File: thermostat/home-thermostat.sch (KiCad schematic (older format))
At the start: 40 parts, among them J1 Thermosthat, U3 LM2574M-5, U4 LD1117S33TR_SOT223, U5 AT24C512

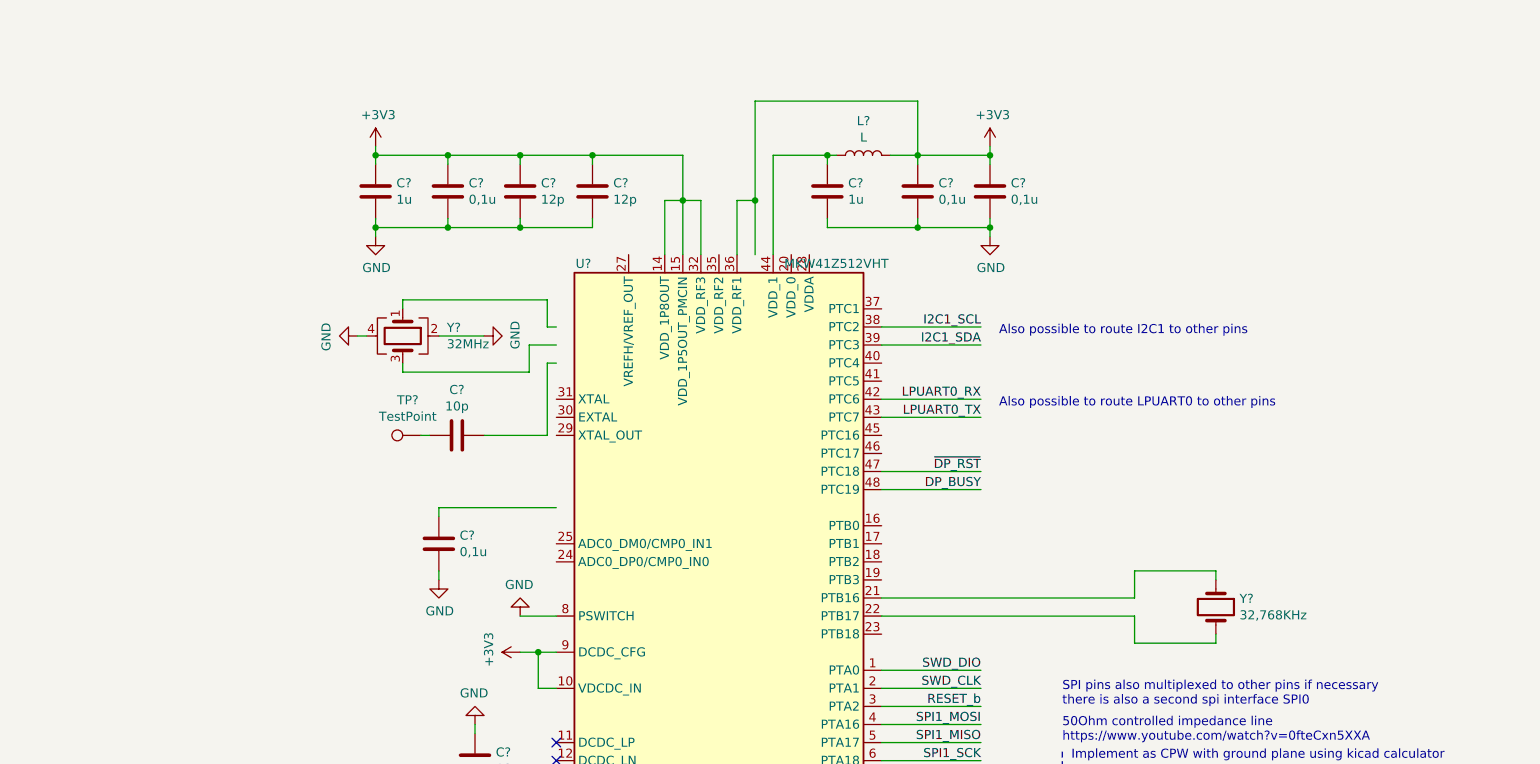
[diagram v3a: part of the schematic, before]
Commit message: Added some descriptions and the possibility to use VDD as reference voltage for the ADC of the MKW41Z. This can come handy if we want to use the ADC to measure voltages.
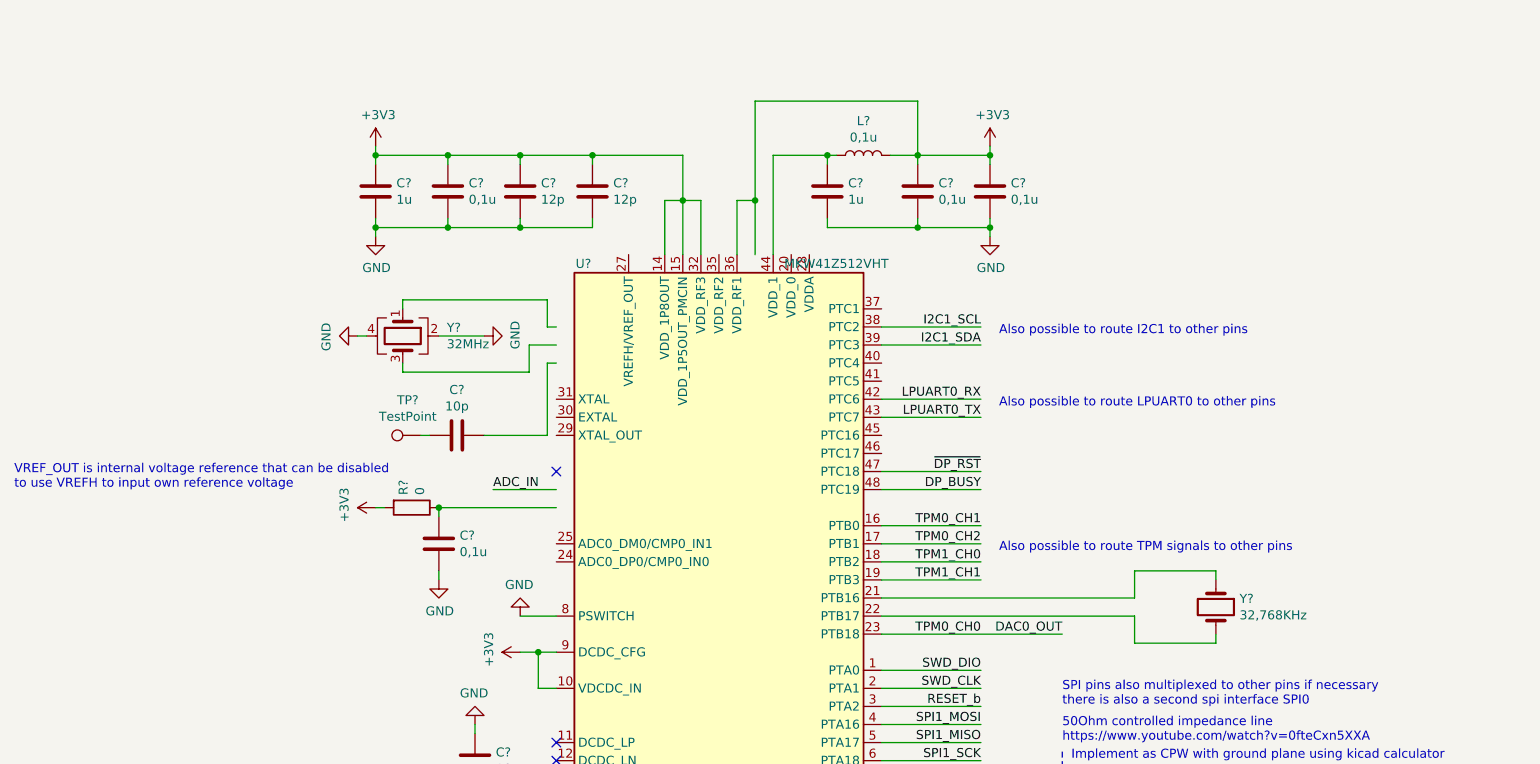
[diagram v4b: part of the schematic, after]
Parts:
- added R?: 0, symbol Device:R
- L?: value L -> 0,1u
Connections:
- net labels added: ADC_IN, DAC0_OUT, TPM0_CH0, TPM0_CH1, TPM0_CH2, TPM1_CH0, TPM1_CH1
- wire segments 189 -> 196
- no-connect marks 2 -> 3
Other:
- note added: "Also possible to route TPM signals to other pins"
- note added: "VREF_OUT is internal voltage reference that can be disabled\nto use VREFH to input own reference voltage"
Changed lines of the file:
@@
 P 6200 1100
 F 0 "L?" V 6390 1100 50  0000 C CNN
-F 1 "L" V 6299 1100 50  0000 C CNN
+F 1 "0,1u" V 6299 1100 50  0000 C CNN
 F 2 "" H 6200 1100 50  0001 C CNN
 F 3 "~" H 6200 1100 50  0001 C CNN
@@
 Wire Wire Line
 	6850 2950 6300 2950
+Text Label 6850 3150 2    50   ~ 0
+TPM0_CH1
+Wire Wire Line
+	6850 3150 6300 3150
+Text Label 6850 3250 2    50   ~ 0
+TPM0_CH2
+Wire Wire Line
+	6850 3250 6300 3250
+Text Label 6850 3350 2    50   ~ 0
+TPM1_CH0
+Wire Wire Line
+	6850 3350 6300 3350
+Text Label 6850 3450 2    50   ~ 0
+TPM1_CH1
+Wire Wire Line
+	6850 3450 6300 3450
+Text Label 6850 3750 2    50   ~ 0
+TPM0_CH0
+Text Label 7300 3750 2    50   ~ 0
+DAC0_OUT
+Wire Wire Line
+	6300 3750 7300 3750
+Text Notes 6950 3300 0    50   ~ 0
+Also possible to route TPM signals to other pins
+Text Label 4150 2950 0    50   ~ 0
+ADC_IN
+Wire Wire Line
+	4150 2950 4500 2950
+NoConn ~ 4500 2850
+$Comp
+L Device:R R?
+U 1 1 5F3B355B
+P 3700 3050
+F 0 "R?" H 3630 3004 50  0000 R CNN
+F 1 "0" H 3630 3095 50  0000 R CNN
+F 2 "" V 3630 3050 50  0001 C CNN
+F 3 "~" H 3700 3050 50  0001 C CNN
+	1    3700 3050
+	0    1    1    0
+$EndComp
+Connection ~ 3850 3050
+$Comp
+L power:+3V3 #PWR?
+U 1 1 5F3B429E
+P 3500 3050
+AR Path="/5E8AC4D3/5F3B429E" Ref="#PWR?"  Part="1"
+AR Path="/5F3B429E" Ref="#PWR?"  Part="1"
+F 0 "#PWR?" H 3500 2900 50  0001 C CNN
+F 1 "+3V3" H 3515 3223 50  0000 C CNN
+F 2 "" H 3500 3050 50  0001 C CNN
+F 3 "" H 3500 3050 50  0001 C CNN
+	1    3500 3050
+	0    -1   -1   0
+$EndComp
+Wire Wire Line
+	3500 3050 3550 3050
+Text Notes 1500 2950 0    50   ~ 0
+VREF_OUT is internal voltage reference that can be disabled\nto use VREFH to input own reference voltage
 $EndSCHEMATC

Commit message: Moved I2C peripherals into one schematic, moved GPIO peripherals onto main schematic.
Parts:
- removed C15: 22u, Capacitor_SMD:C_0805_2012Metric, symbol Device:C
- removed C16: 100n, Capacitor_SMD:C_0603_1608Metric, symbol Device:C
- removed C19: 2u2, Capacitor_SMD:C_0603_1608Metric, symbol Device:C
- removed C20: 220u, Capacitor_SMD:CP_Elec_6.3x5.4, symbol Device:C
- removed C30: 10n, Capacitor_SMD:C_0603_1608Metric, symbol Device:C
- removed D4: SL03, Diode_SMD:D_SMF, symbol Device:D_Schottky
- removed J1: Thermosthat, Connector_PinHeader_2.54mm:PinHeader_1x03_P2.54mm_Vertical_SMD_Pin1Left, symbol Connector_Generic:Conn_01x03
- removed L2: 330u, Inductor_SMD:L_7.3x7.3_H3.5, symbol Device:L_Core_Iron
- removed U3: LM2574M-5, Package_SO:SOIC-14W_7.5x9mm_P1.27mm, symbol Regulator_Switching:LM2574M-5
- removed U4: LD1117S33TR_SOT223, Package_TO_SOT_SMD:SOT-223-3_TabPin2, symbol Regulator_Linear:LD1117S33TR_SOT223
- removed U5: AT24C512, Package_DIP:DIP-8_W7.62mm_SMDSocket_SmallPads, symbol Memory_EEPROM:CAT24C256
- added C? (x6): 1n, symbol Device:C
- added D?: YELLOW, LED_SMD:LED_1210_3225Metric, symbol Device:LED
- added D?: RED, LED_SMD:LED_1210_3225Metric, symbol Device:LED
- added D?: GREEN, LED_SMD:LED_1210_3225Metric, symbol Device:LED
- added Q? (x3): BC817, Package_TO_SOT_SMD:SOT-23, symbol Device:Q_NPN_BEC
- added R? (x3): 0, Resistor_SMD:R_0603_1608Metric, symbol Device:R
- added SW?: UP, Button_Switch_SMD:SW_SPST_Panasonic_EVQPL_3PL_5PL_PT_A08, symbol Switch:SW_Push
- added SW?: DOWN, Button_Switch_SMD:SW_SPST_Panasonic_EVQPL_3PL_5PL_PT_A08, symbol Switch:SW_Push
- added SW?: LEFT, Button_Switch_SMD:SW_SPST_Panasonic_EVQPL_3PL_5PL_PT_A08, symbol Switch:SW_Push
- added SW?: RIGHT, Button_Switch_SMD:SW_SPST_Panasonic_EVQPL_3PL_5PL_PT_A08, symbol Switch:SW_Push
- added SW?: OK, Button_Switch_SMD:SW_SPST_Panasonic_EVQPL_3PL_5PL_PT_A08, symbol Switch:SW_Push
- added SW?: CANCEL, Button_Switch_SMD:SW_SPST_Panasonic_EVQPL_3PL_5PL_PT_A08, symbol Switch:SW_Push
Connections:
- net labels added: CANCEL, DOWN, LED_GREEN, LED_OUT, LED_RED, LEFT, OK, RIGHT, UP
- net labels removed: +36V, +5V, 8, 9, AVR_INT, GNDA, SCL, SDA, regulator_out
- wire segments 196 -> 181
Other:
- note added: "1,8V, 2mA"
- note added: "Button matrix for basic input\nif WIFI is not available"
- note added: "Jumper select if PWM or DAC is used"
- note added: "Signal LED with PWM option"
- note removed: "20V, 1A, E-LAB"
- note removed: "3,3V is generated with an LDO fixed voltage supply"
- note removed: "7-8-9 Port for Thermosthat control"
- note removed: "EEPROM for off-ESP config"
- note removed: "Step-Down converter to transform variable ~~30V supply to 5V"

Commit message: Put LEDs and GPIOs into separate schematic, GPIO for arrow buttons are now attached over an expander.
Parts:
- removed C? (x6): 1n, symbol Device:C
- removed D?: YELLOW, LED_SMD:LED_1210_3225Metric, symbol Device:LED
- removed D?: RED, LED_SMD:LED_1210_3225Metric, symbol Device:LED
- removed D?: GREEN, LED_SMD:LED_1210_3225Metric, symbol Device:LED
- removed Q? (x3): BC817, Package_TO_SOT_SMD:SOT-23, symbol Device:Q_NPN_BEC
- removed R? (x3): 0, Resistor_SMD:R_0603_1608Metric, symbol Device:R
- removed SW?: UP, Button_Switch_SMD:SW_SPST_Panasonic_EVQPL_3PL_5PL_PT_A08, symbol Switch:SW_Push
- removed SW?: DOWN, Button_Switch_SMD:SW_SPST_Panasonic_EVQPL_3PL_5PL_PT_A08, symbol Switch:SW_Push
- removed SW?: LEFT, Button_Switch_SMD:SW_SPST_Panasonic_EVQPL_3PL_5PL_PT_A08, symbol Switch:SW_Push
- removed SW?: RIGHT, Button_Switch_SMD:SW_SPST_Panasonic_EVQPL_3PL_5PL_PT_A08, symbol Switch:SW_Push
- removed SW?: OK, Button_Switch_SMD:SW_SPST_Panasonic_EVQPL_3PL_5PL_PT_A08, symbol Switch:SW_Push
- removed SW?: CANCEL, Button_Switch_SMD:SW_SPST_Panasonic_EVQPL_3PL_5PL_PT_A08, symbol Switch:SW_Push
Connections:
- net labels added: BTN_CANCEL, BTN_OK, TPM0_CH3, TPM2_CH0, TPM2_CH1, ~BTN_INT
- net labels removed: CANCEL, DOWN, LED_GREEN, LED_OUT, LED_RED, LEFT, OK, RIGHT, UP
- wire segments 181 -> 154
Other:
- note removed: "1,8V, 2mA"
- note removed: "Button matrix for basic input\nif WIFI is not available"
- note removed: "MKW41Z internal pullups can be activated for I2C\nHowever, the pull resistors are disabled whenever the output buffer is enabled?"
- note removed: "Signal LED with PWM option"

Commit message: Fixed orphaned symbols after Kicad library update. Kinetis MCU is now in upstream, thanks to me :)
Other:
- note removed: "Jumper select if PWM or DAC is used"
- note removed: "Will we do peripherals with AVR or does MKW41Z has enough free pins?\nDo we want to try touch interface with MKW41 or AVR?"
- moved on the sheet: C?, L?, R?, TP?, Y?

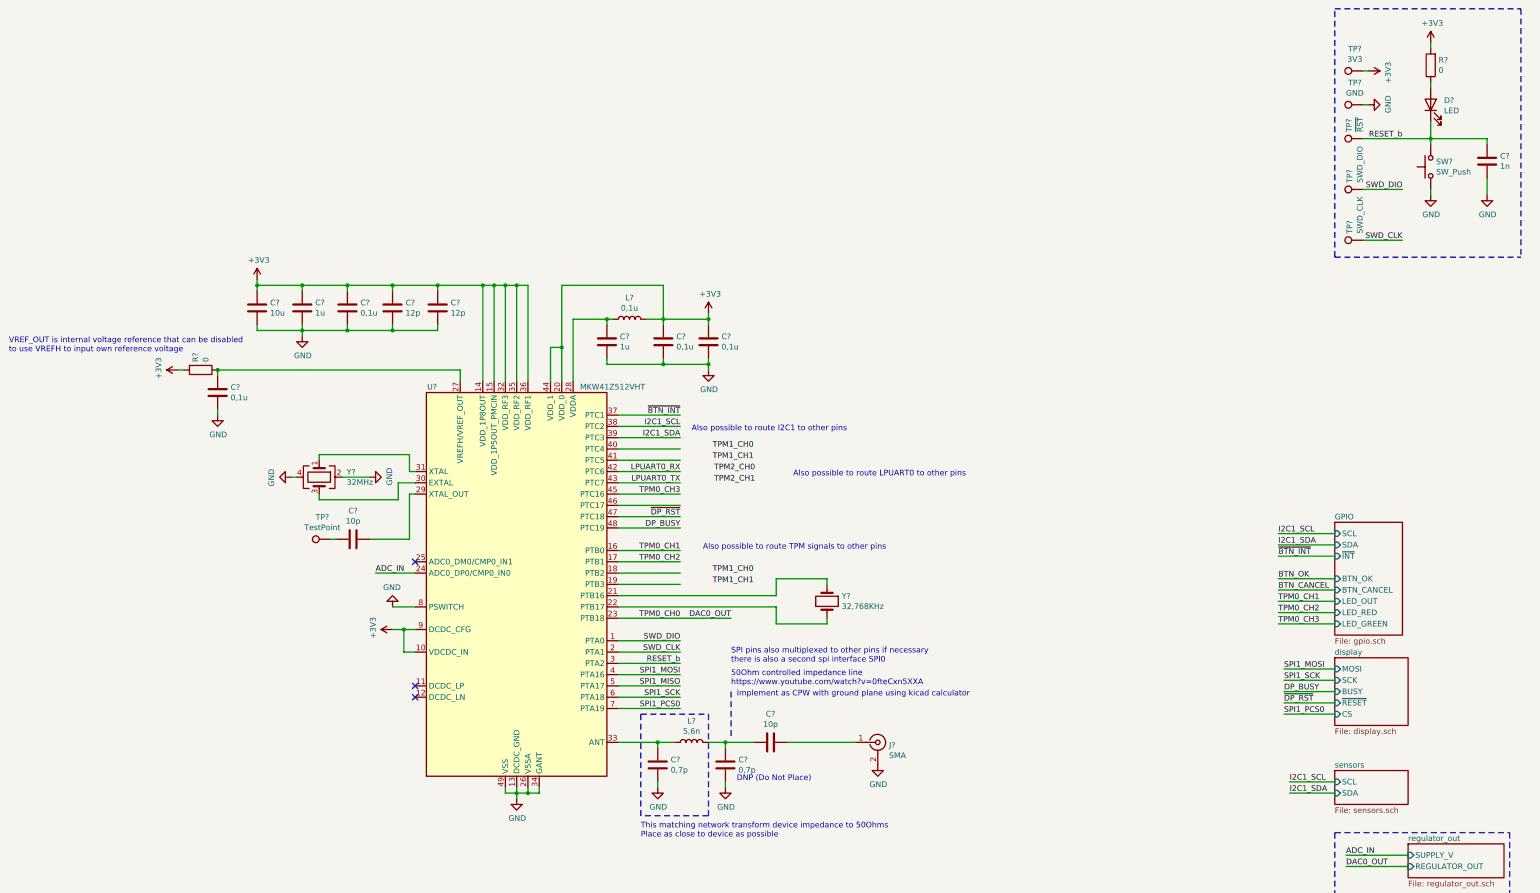
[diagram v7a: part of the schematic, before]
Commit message: Updated symbols after library update, some footprints still need to be assigned. Deleted PCB except for Display and buttons. Button arrangement wrong. Move buttons to other side of Display. Maybe put buttons on separate PCB and create one PCB for MCU and logic, since that needs to be a four layer one. That is expensive and should be kept as small as possible.
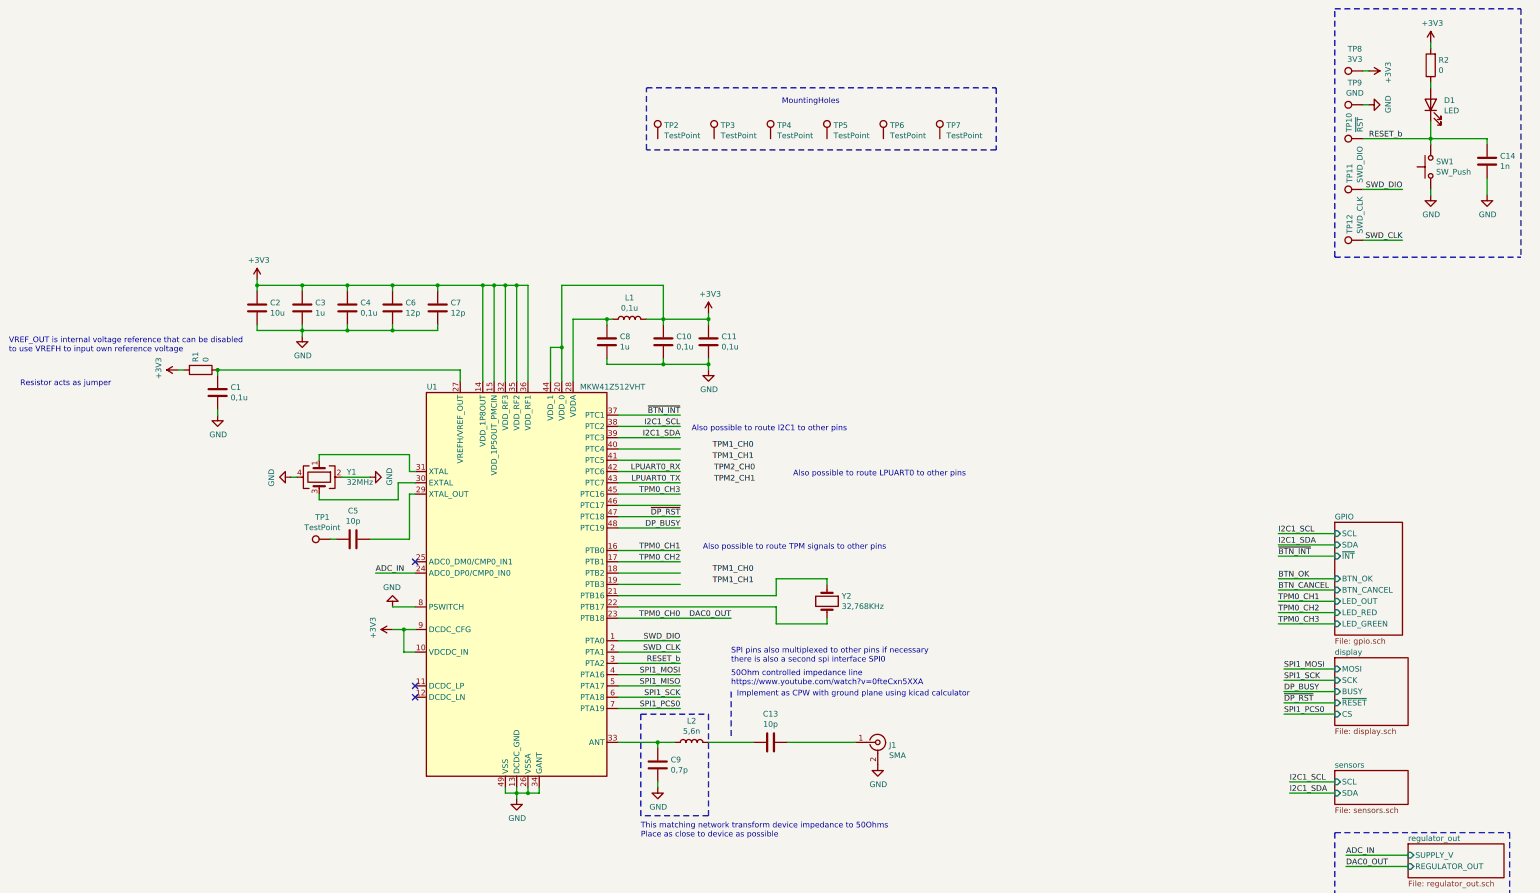
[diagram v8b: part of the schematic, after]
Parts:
- removed C?: 0,7p, symbol Device:C
- added TP2, TP3, TP4, TP5, TP6, TP7: TestPoint, MountingHole:MountingHole_3.2mm_M3, symbol Connector:TestPoint
- C14: renamed from C?; footprint (none) -> Capacitor_SMD:C_0603_1608Metric
- D1: renamed from D?; footprint (none) -> LED_SMD:LED_1210_3225Metric
- R1, R2: renamed from R?; footprint (none) -> Resistor_SMD:R_0603_1608Metric
- SW1: renamed from SW?; footprint (none) -> Button_Switch_SMD:SW_SPST_Panasonic_EVQPL_3PL_5PL_PT_A08
- TP1, TP10, TP11, TP12, TP8, TP9: renamed from TP?; footprint (none) -> TestPoint:TestPoint_Pad_D1.0mm
- gave numbers to parts that had none: 18
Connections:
- wire segments 154 -> 151
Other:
- note added: "MountingHoles\n"
- note added: "Resistor acts as jumper"
- note removed: "DNP (Do Not Place)"
